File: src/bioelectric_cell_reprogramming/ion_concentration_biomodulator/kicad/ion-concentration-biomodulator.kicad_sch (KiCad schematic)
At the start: 54 parts, among them J1 532610671, J10 39-53-2045, J11 Conn_01x14_Pin, J12 Conn_01x14_Pin, J13 39-53-2045, J14 39-53-2045, J15 Conn_ARM_SWD_TagConnect_TC2030, J16 IPL1-104-01-L-D-K, J17 Conn_01x02_Pin, J18 EJ508A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

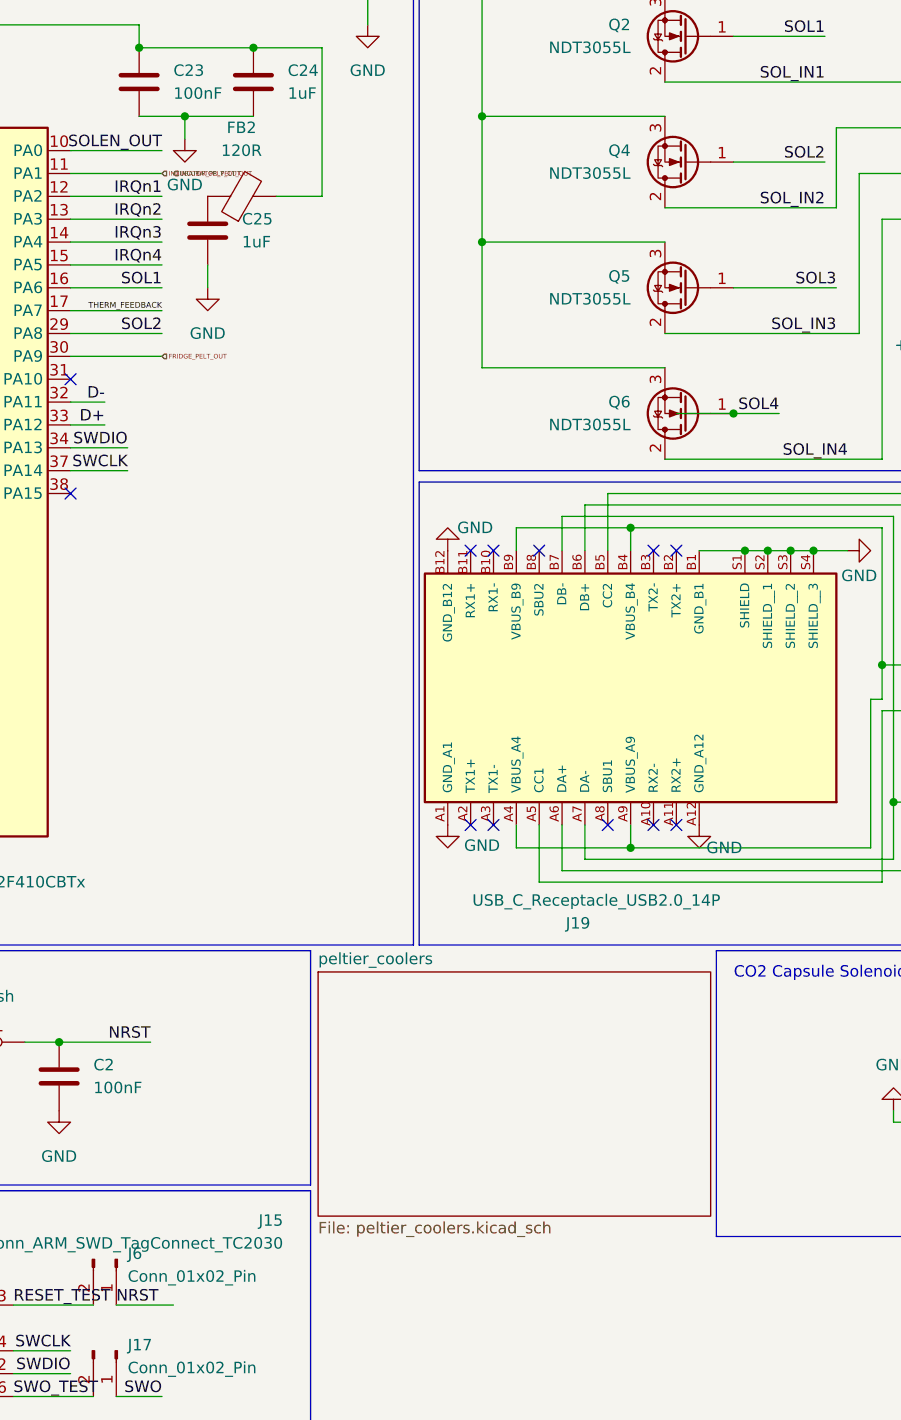
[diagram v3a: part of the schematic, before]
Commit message: fix: ERC errors
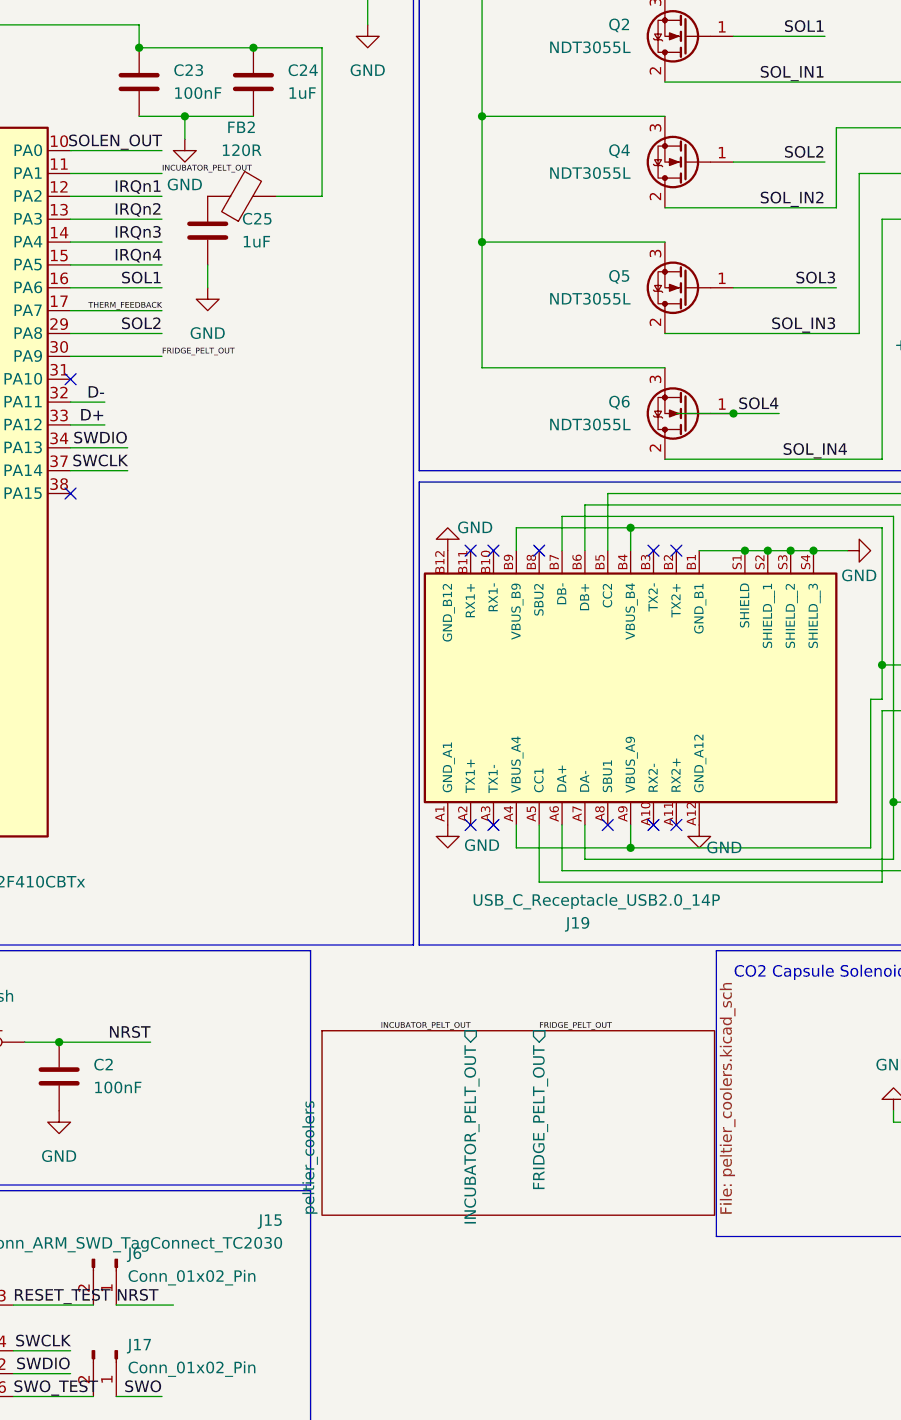
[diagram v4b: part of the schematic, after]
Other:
- sheet peltier_coolers ports: added FRIDGE_PELT_OUT, INCUBATOR_PELT_OUT; removed none
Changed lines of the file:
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@@
 		)
 	)
+	(label "INCUBATOR_PELT_OUT"
+		(at 160.02 46.99 0)
+		(fields_autoplaced yes)
+		(effects
+			(font
+				(size 0.635 0.635)
+			)
+			(justify left bottom)
+		)
+	)
 	(label "I2C_SDA"
 		(at 24.13 213.36 0)
@@
 		)
 	)
+	(label "INCUBATOR_PELT_OUT"
+		(at 194.31 142.24 180)
+		(fields_autoplaced yes)
+		(effects
+			(font
+				(size 0.635 0.635)
+			)
+			(justify right bottom)
+		)
+	)
 	(label "SOLEN_OUT"
 		(at 247.65 138.43 0)
@@
 		)
 	)
+	(label "FRIDGE_PELT_OUT"
+		(at 201.93 142.24 0)
+		(fields_autoplaced yes)
+		(effects
+			(font
+				(size 0.635 0.635)
+			)
+			(justify left bottom)
+		)
+	)
 	(label "SOL3"
 		(at 234.95 59.69 180)
@@
 		)
 	)
+	(label "FRIDGE_PELT_OUT"
+		(at 160.02 67.31 0)
+		(fields_autoplaced yes)
+		(effects
+			(font
+				(size 0.635 0.635)
+			)
+			(justify left bottom)
+		)
+	)
 	(label "32+"
 		(at 48.26 170.18 0)
@@
 		)
 	)
-	(hierarchical_label "FRIDGE_PELT_OUT"
-		(shape input)
-		(at 160.02 67.31 0)
-		(fields_autoplaced yes)
-		(effects
-			(font
-				(size 0.508 0.508)
-			)
-			(justify left)
-		)
-	)
-	(hierarchical_label "INCUBATOR_PELT_OUT"
-		(shape input)
-		(at 161.29 46.99 0)
-		(fields_autoplaced yes)
-		(effects
-			(font
-				(size 0.508 0.508)
-			)
-			(justify left)
-		)
-	)
-	(hierarchical_label "INCUBATOR_PELT_OUT"
-		(shape input)
-		(at 160.02 46.99 0)
-		(fields_autoplaced yes)
-		(effects
-			(font
-				(size 0.508 0.508)
-			)
-			(justify left)
-		)
-	)
 	(symbol
 		(lib_id "2024-08-13_01-50-37:IPL1-104-01-L-D-K")
@@
 	)
 	(sheet
-		(at 177.3682 135.7122)
-		(size 43.6118 27.1272)
+		(at 177.8 142.24)
+		(size 43.6118 20.4978)
 		(fields_autoplaced yes)
 		(stroke
@@
 		)
 		(property "Sheetname" "peltier_coolers"
-			(at 177.3682 135.0006 0)
+			(at 177.0884 162.7378 90)
 			(effects
 				(font
@@
 		)
 		(property "Sheetfile" "peltier_coolers.kicad_sch"
-			(at 177.3682 163.424 0)
+			(at 221.9964 162.7378 90)
 			(effects
 				(font
@@
 			)
 		)
+		(pin "INCUBATOR_PELT_OUT" input
+			(at 194.31 142.24 90)
+			(effects
+				(font
+					(size 1.27 1.27)
+				)
+				(justify right)
+			)
+		)
+		(pin "FRIDGE_PELT_OUT" input
+			(at 201.93 142.24 90)
+			(effects
+				(font
+					(size 1.27 1.27)
+				)
+				(justify right)
+			)
+		)

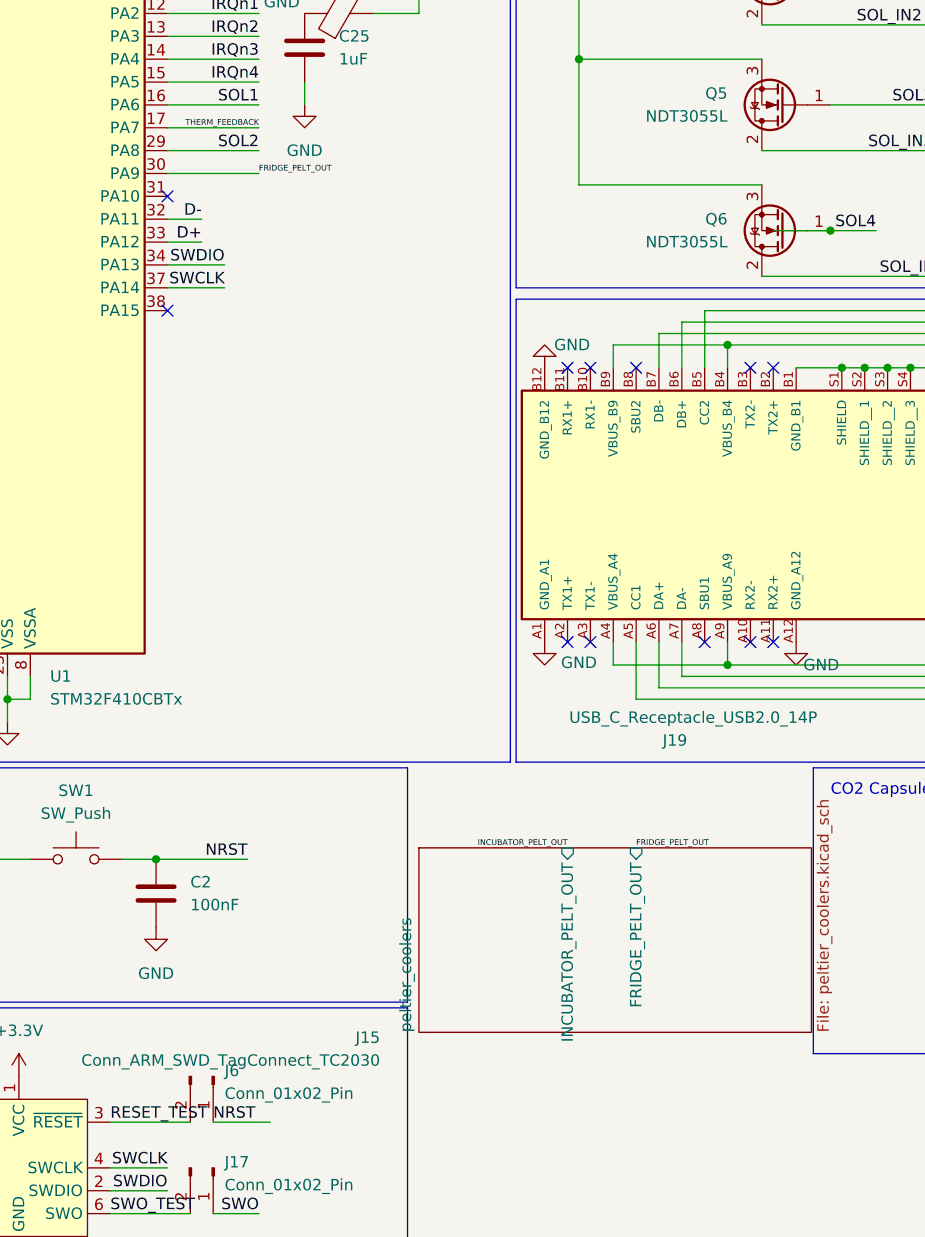
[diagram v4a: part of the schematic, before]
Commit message: fix: replace fridge peltier cooler FET with an h-bridge
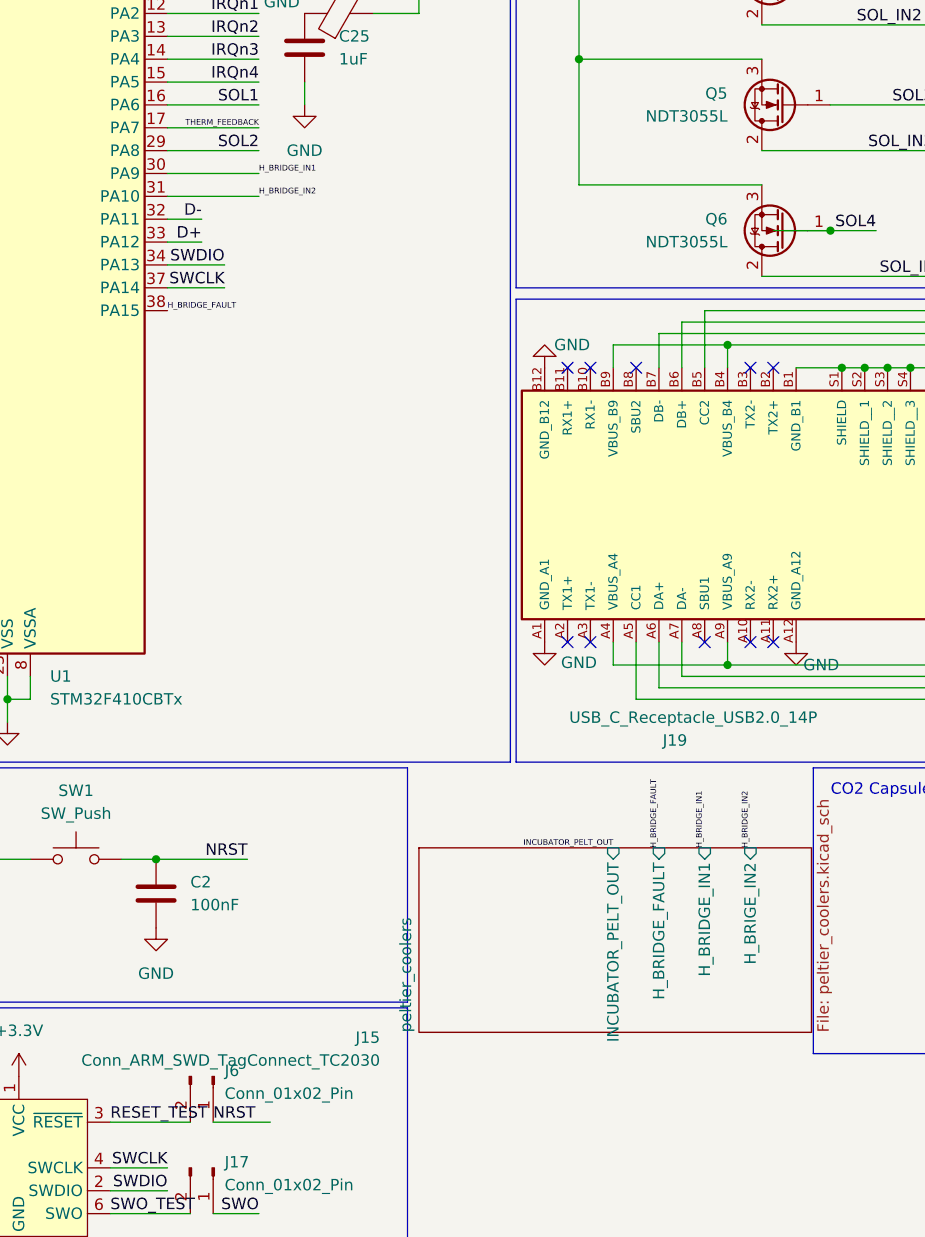
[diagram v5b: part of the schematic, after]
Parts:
- R6: footprint Resistor_SMD:R_0603_1608Metric -> Resistor_SMD:R_0201_0603Metric
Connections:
- net H_BRIDGE_IN2: now reaches U1.31 (PA10)
- net H_BRIDGE_FAULT: now reaches U1.38 (PA15)
- net FRIDGE_PELT_OUT renamed H_BRIDGE_IN1
- no-connect marks 37 -> 35
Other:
- sheet peltier_coolers ports: added H_BRIDGE_FAULT, H_BRIDGE_IN1, H_BRIGE_IN2; removed FRIDGE_PELT_OUT
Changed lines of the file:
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@@
 	)
 	(no_connect
-		(at 149.86 82.55)
-	)
-	(no_connect
 		(at 74.93 154.94)
 	)
@@
 	)
 	(no_connect
-		(at 149.86 69.85)
-	)
-	(no_connect
 		(at 82.55 256.54)
 	)
@@
 	(wire
 		(pts
+			(xy 149.86 69.85) (xy 160.02 69.85)
+		)
+		(stroke
+			(width 0)
+			(type default)
+		)
+	)
+	(wire
+		(pts
 			(xy 88.9 95.25) (xy 95.25 95.25)
 		)
@@
 		)
 	)
+	(label "H_BRIDGE_FAULT"
+		(at 204.47 142.24 90)
+		(fields_autoplaced yes)
+		(effects
+			(font
+				(size 0.635 0.635)
+			)
+			(justify left bottom)
+		)
+	)
 	(label "I2C_SCK"
 		(at 100.33 104.14 0)
@@
 	)
 	(label "INCUBATOR_PELT_OUT"
-		(at 194.31 142.24 180)
+		(at 199.39 142.24 180)
 		(fields_autoplaced yes)
 		(effects
@@
 		)
 	)
+	(label "H_BRIDGE_FAULT"
+		(at 149.86 82.55 0)
+		(fields_autoplaced yes)
+		(effects
+			(font
+				(size 0.635 0.635)
+			)
+			(justify left bottom)
+		)
+	)
 	(label "NRST"
 		(at 111.76 44.45 0)
@@
 		)
 	)
+	(label "H_BRIDGE_IN2"
+		(at 214.63 142.24 90)
+		(fields_autoplaced yes)
+		(effects
+			(font
+				(size 0.635 0.635)
+			)
+			(justify left bottom)
+		)
+	)
 	(label "NRST"
 		(at 154.94 172.72 0)
@@
 		)
 	)
-	(label "FRIDGE_PELT_OUT"
-		(at 201.93 142.24 0)
+	(label "H_BRIDGE_IN2"
+		(at 160.02 69.85 0)
 		(fields_autoplaced yes)
 		(effects
@@
 		)
 	)
-	(label "FRIDGE_PELT_OUT"
-		(at 160.02 67.31 0)
+	(label "32+"
+		(at 48.26 170.18 0)
 		(fields_autoplaced yes)
 		(effects
 			(font
-				(size 0.635 0.635)
+				(size 1.27 1.27)
 			)
 			(justify left bottom)
 		)
 	)
-	(label "32+"
-		(at 48.26 170.18 0)
+	(label "H_BRIDGE_IN1"
+		(at 160.02 67.31 0)
 		(fields_autoplaced yes)
 		(effects
 			(font
-				(size 1.27 1.27)
+				(size 0.635 0.635)
 			)
 			(justify left bottom)
@@
 		)
 	)
+	(label "H_BRIDGE_IN1"
+		(at 209.55 142.24 90)
+		(fields_autoplaced yes)
+		(effects
+			(font
+				(size 0.635 0.635)
+			)
+			(justify left bottom)
+		)
+	)
 	(symbol
 		(lib_id "2024-08-13_01-50-37:IPL1-104-01-L-D-K")
@@
 			)
 		)
-		(property "Footprint" "Resistor_SMD:R_0603_1608Metric"
+		(property "Footprint" "Resistor_SMD:R_0201_0603Metric"
 			(at 191.77 220.218 90)
 			(effects
@@
 		)
 		(pin "INCUBATOR_PELT_OUT" input
-			(at 194.31 142.24 90)
+			(at 199.39 142.24 90)
+			(effects
+				(font
+					(size 1.27 1.27)
+				)
+				(justify right)
+			)
+		)
+		(pin "H_BRIDGE_FAULT" input
+			(at 204.47 142.24 90)
+			(effects
+				(font
+					(size 1.27 1.27)
+				)
+				(justify right)
+			)
+		)
+		(pin "H_BRIDGE_IN1" input
+			(at 209.55 142.24 90)
 			(effects
 				(font
@@
 			)
 		)
-		(pin "FRIDGE_PELT_OUT" input
-			(at 201.93 142.24 90)
+		(pin "H_BRIGE_IN2" input
+			(at 214.63 142.24 90)
 			(effects
 				(font
